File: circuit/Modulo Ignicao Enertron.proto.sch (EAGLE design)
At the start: 36 parts, among them IC1 PIC12F675P, IC2 78L05, K1 ISP, P1 5k, Q1 IRGB14C40L

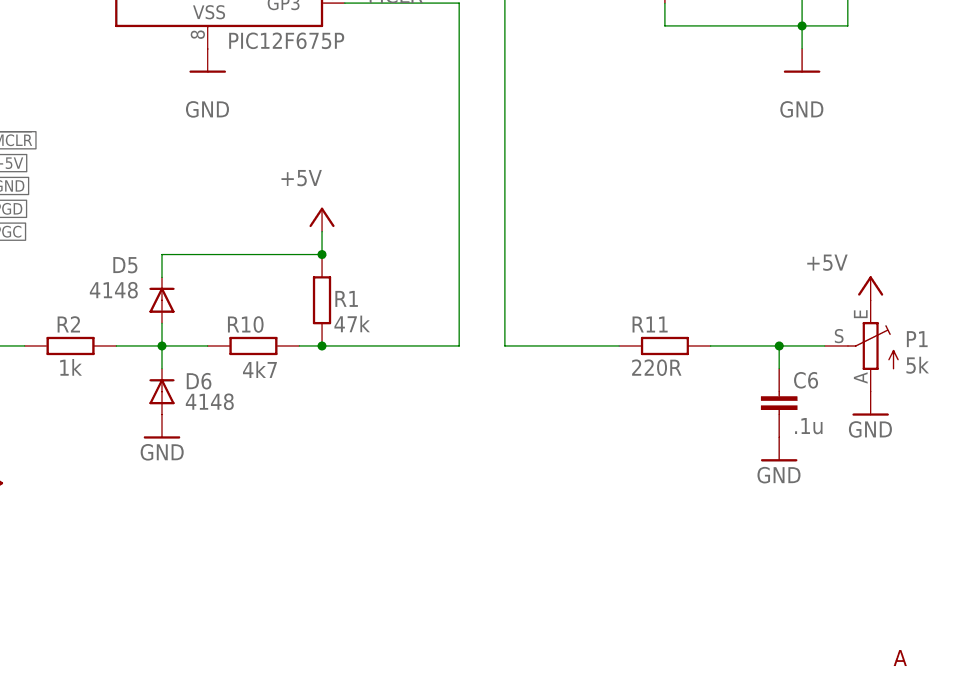
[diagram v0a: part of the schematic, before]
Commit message: Corrected circuit around MCLR
Corrected circuit around MCLR pin to allow ICSP. The diode network was
bypassing MCLR high voltage to VCC. A series resistor fixed the problem.
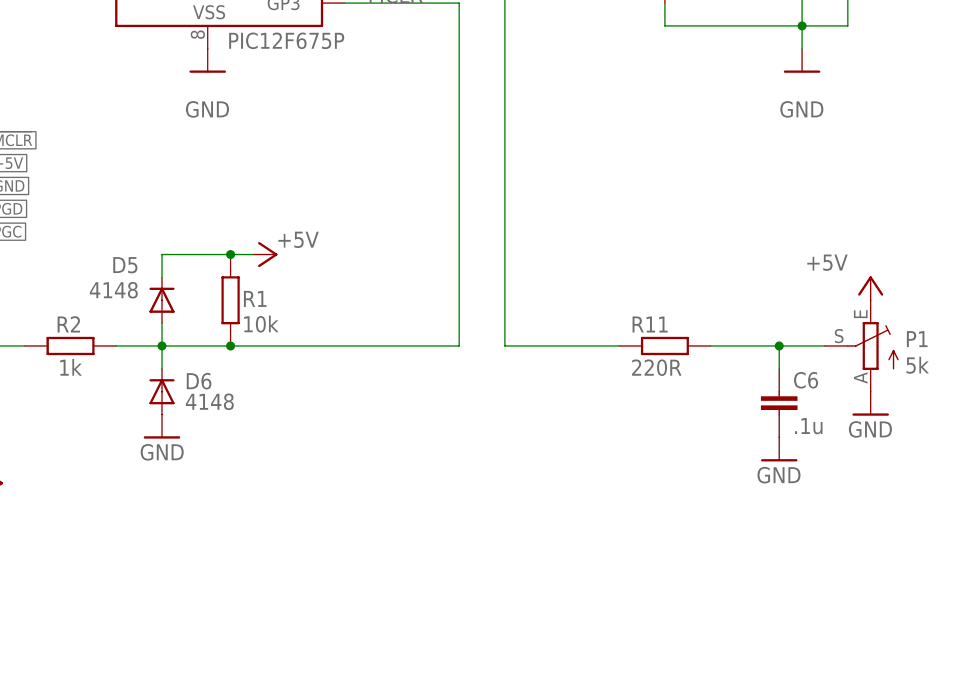
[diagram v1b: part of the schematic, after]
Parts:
- removed R10: 4k7, rcl:R-EU_0207/7L
- R1: value 47k -> 10k
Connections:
- removed net N$4: D5.A, D6.C, R10.1, R2.1
- net !MCLR: now also D5.A, D6.C, R2.1; no longer R10.2
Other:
- note removed: "A"
- moved on the sheet: R1
